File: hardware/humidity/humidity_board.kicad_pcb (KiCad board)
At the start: 2 copper layers, 139 x 20 mm, 23 parts, among them IC1 ATMEGA88-A, J1 RJ45, P1 ISP, P2 UART, SW1 SW_RESET, U1 ST485, U2 HYT271, m3_loch VAL**

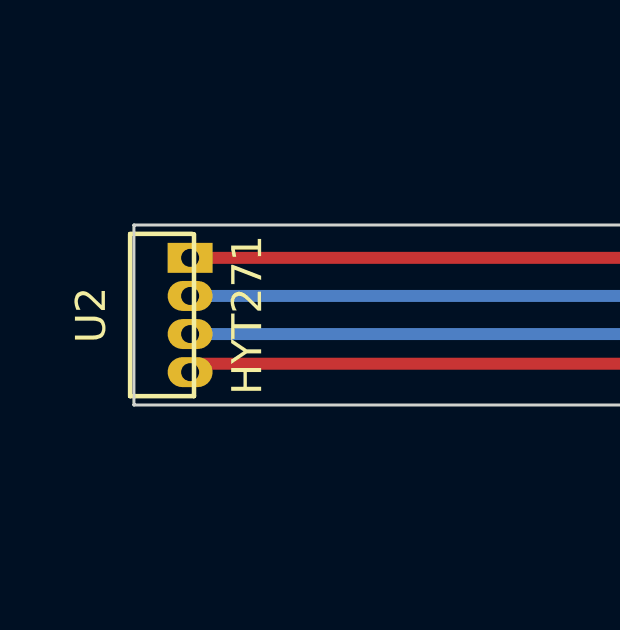
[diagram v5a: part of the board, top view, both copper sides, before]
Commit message: change sensor modules
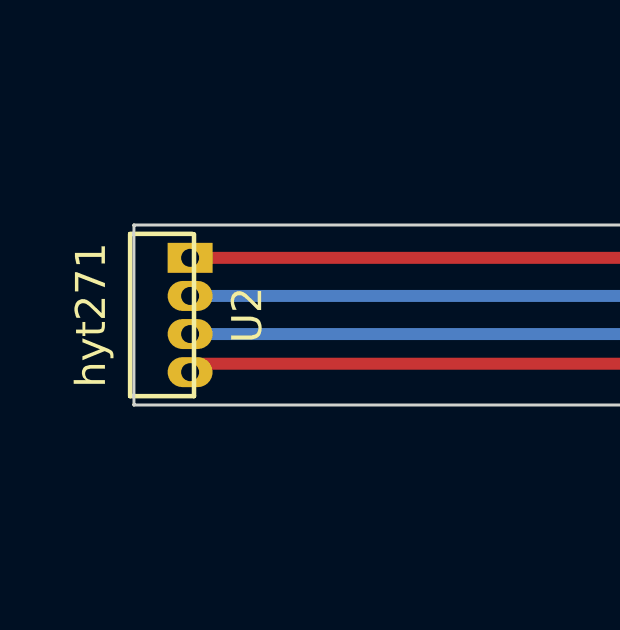
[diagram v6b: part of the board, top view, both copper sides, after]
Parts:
- removed U2: HYT271, HYT271
- added hyt271: U2, HYT271, F.Cu at (80.5, 96.0)
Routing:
- net /SCL: track 52.9 -> 0.00 mm
- net (no net): track 0.00 -> 52.9 mm
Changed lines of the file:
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@@
 (kicad_pcb (version 3) (host pcbnew "(2013-may-18)-stable")
   (general
-    (links 62)
+    (links 58)
     (no_connects 0)
-    (area 7.399999 79.150001 244.600001 118.7)
+    (area 7.399999 74 244.600001 118.7)
     (thickness 1.6)
     (drawings 12)
@@
     (mod_text_size 1 1)
     (mod_text_width 0.15)
-    (pad_size 1 1.5)
+    (pad_size 1 1.7)
     (pad_drill 0.6)
     (pad_to_mask_clearance 0)
@@
     )
   )
+  (module m3_loch (layer F.Cu)
+    (at 187.5 101)
+    (fp_text reference m3_loch (at 0 -5.588) (layer F.SilkS)
+      (effects (font (size 1 1) (thickness 0.15)))
+    )
+    (fp_text value VAL** (at 0 5.842) (layer F.SilkS)
+      (effects (font (size 1 1) (thickness 0.15)))
+    )
+    (pad "" np_thru_hole circle (at 0 0) (size 3.4 3.4) (drill 3.4)
+      (layers *.Cu *.Mask F.SilkS)
+      (clearance 3.3)
+    )
+  )
+  (module m3_loch (layer F.Cu)
+    (at 125.5 91)
+    (fp_text reference m3_loch (at 0 -5.588) (layer F.SilkS)
+      (effects (font (size 1 1) (thickness 0.15)))
+    )
+    (fp_text value VAL** (at 0 5.842) (layer F.SilkS)
+      (effects (font (size 1 1) (thickness 0.15)))
+    )
+    (pad "" np_thru_hole circle (at 0 0) (size 3.4 3.4) (drill 3.4)
+      (layers *.Cu *.Mask F.SilkS)
+      (clearance 3.3)
+    )
+  )
   (module HYT271 (layer F.Cu)
     (at 80.5 96 270)
-    (fp_text reference U2 (at 0 3.429 270) (layer F.SilkS)
+    (fp_text reference hyt271 (at 0 3.429 270) (layer F.SilkS)
       (effects (font (size 1 1) (thickness 0.15)))
     )
-    (fp_text value HYT271 (at 0 -1.778 270) (layer F.SilkS)
+    (fp_text value U2 (at 0 -1.778 270) (layer F.SilkS)
       (effects (font (size 1 1) (thickness 0.15)))
     )
@@
     (pad 2 thru_hole oval (at -0.635 0.127 270) (size 1 1.5) (drill 0.6)
       (layers *.Cu *.Mask F.SilkS)
-      (net 14 GND)
     )
     (pad 3 thru_hole oval (at 0.635 0.127 270) (size 1 1.5) (drill 0.6)
       (layers *.Cu *.Mask F.SilkS)
-      (net 18 VCC)
     )
     (pad 4 thru_hole oval (at 1.905 0.127 270) (size 1 1.5) (drill 0.6)
       (layers *.Cu *.Mask F.SilkS)
-      (net 9 /SCL)
     )
     (pad 1 thru_hole trapezoid (at -1.905 0.127 270) (size 1 1.5) (drill 0.6)
       (layers *.Cu *.Mask F.SilkS)
-      (net 10 /SDA)
-    )
-  )
-  (module m3_loch (layer F.Cu)
-    (at 187.5 101)
-    (fp_text reference m3_loch (at 0 -5.588) (layer F.SilkS)
-      (effects (font (size 1 1) (thickness 0.15)))
-    )
-    (fp_text value VAL** (at 0 5.842) (layer F.SilkS)
-      (effects (font (size 1 1) (thickness 0.15)))
-    )
-    (pad "" np_thru_hole circle (at 0 0) (size 3.4 3.4) (drill 3.4)
-      (layers *.Cu *.Mask F.SilkS)
-      (clearance 3.3)
-    )
-  )
-  (module m3_loch (layer F.Cu)
-    (at 125.5 91)
-    (fp_text reference m3_loch (at 0 -5.588) (layer F.SilkS)
-      (effects (font (size 1 1) (thickness 0.15)))
-    )
-    (fp_text value VAL** (at 0 5.842) (layer F.SilkS)
-      (effects (font (size 1 1) (thickness 0.15)))
-    )
-    (pad "" np_thru_hole circle (at 0 0) (size 3.4 3.4) (drill 3.4)
-      (layers *.Cu *.Mask F.SilkS)
-      (clearance 3.3)
     )
   )
@@
   )
   (gr_line (start 244.5 96) (end 7.5 96) (angle 90) (layer Cmts.User) (width 0.2))
+  (segment (start 133.174 97.62408) (end 80.65392 97.62408) (width 0.4) (layer F.Cu) (net 0) (status 20))
+  (segment (start 80.65392 97.62408) (end 80.373 97.905) (width 0.4) (layer F.Cu) (net 0) (status 30))
   (segment (start 142.7752 100.032) (end 144.032 100.032) (width 0.4) (layer F.Cu) (net 1))
   (segment (start 164.098 97.902) (end 163.5 98.5) (width 0.7) (layer F.Cu) (net 1))
@@
   (segment (start 144.5 92) (end 144.5 97) (width 0.7) (layer B.Cu) (net 8))
   (segment (start 144 91.5) (end 144.5 92) (width 0.7) (layer B.Cu) (net 8))
-  (segment (start 133.174 97.62408) (end 80.65392 97.62408) (width 0.4) (layer F.Cu) (net 9) (status 20))
-  (segment (start 80.65392 97.62408) (end 80.373 97.905) (width 0.4) (layer F.Cu) (net 9) (status 30))
   (segment (start 133.174 96.82652) (end 122.82652 96.82652) (width 0.4) (layer F.Cu) (net 10))
   (segment (start 120.095 94.095) (end 80.373 94.095) (width 0.4) (layer F.Cu) (net 10) (status 20))
@@
   (segment (start 142.782 89.392) (end 143.5 89.392) (width 0.7) (layer F.Cu) (net 17))
   (segment (start 141.945 88.555) (end 142.782 89.392) (width 0.7) (layer F.Cu) (net 17))
-  (segment (start 165.4 96.632) (end 167.632 96.632) (width 0.7) (layer F.Cu) (net 18) (status 400000))
+  (segment (start 165.4 96.632) (end 167.632 96.632) (width 0.7) (layer F.Cu) (net 18))
   (segment (start 167.632 96.632) (end 168.5 97.5) (width 0.7) (layer F.Cu) (net 18))
-  (segment (start 165.4 95.362) (end 167.762 95.362) (width 0.7) (layer F.Cu) (net 18) (status 400000))
+  (segment (start 165.4 95.362) (end 167.762 95.362) (width 0.7) (layer F.Cu) (net 18))
   (segment (start 167.762 95.362) (end 168.5 96.1) (width 0.7) (layer F.Cu) (net 18))
-  (segment (start 171.7 94.092) (end 168.908 94.092) (width 0.7) (layer F.Cu) (net 18) (status 400000))
+  (segment (start 171.7 94.092) (end 168.908 94.092) (width 0.7) (layer F.Cu) (net 18))
   (segment (start 168.908 94.092) (end 168.5 94.5) (width 0.7) (layer F.Cu) (net 18))
-  (segment (start 171.5 91.608) (end 169.092 91.608) (width 0.7) (layer F.Cu) (net 18) (status 400000))
+  (segment (start 171.5 91.608) (end 169.092 91.608) (width 0.7) (layer F.Cu) (net 18))
   (segment (start 169.092 91.608) (end 168.5 92.2) (width 0.7) (layer F.Cu) (net 18))
   (segment (start 169 101) (end 169 98.4) (width 0.7) (layer F.Cu) (net 18))

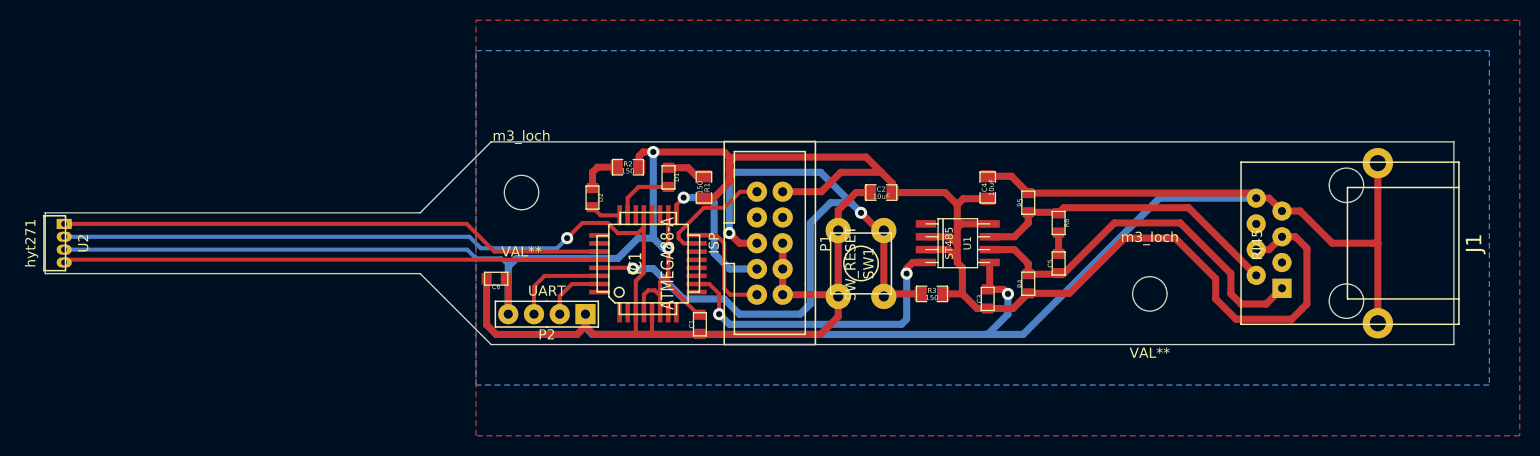
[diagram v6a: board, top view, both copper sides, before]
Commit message: change humidity
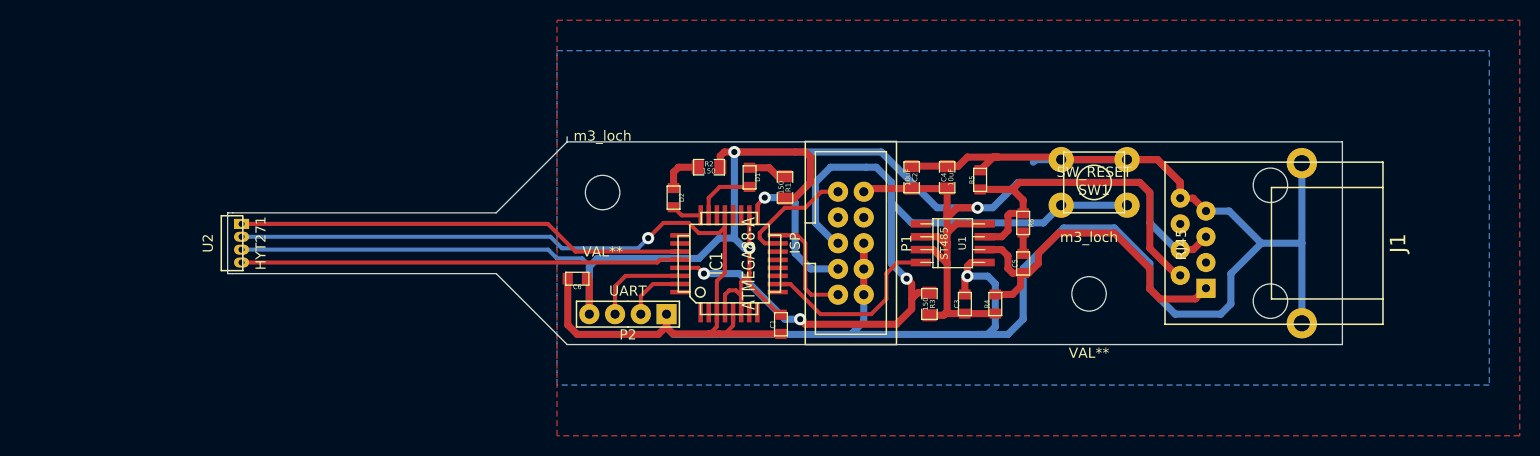
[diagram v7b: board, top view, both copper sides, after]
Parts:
- removed hyt271: U2, HYT271
- added U2: HYT271, HYT271, F.Cu at (98.0, 96.0)
- moved SW1 24.4 mm to (182.0, 90.0), turned to 180 degrees
- moved C1 8.00 mm to (151.1, 104.0)
- moved C6 8.00 mm to (131.0, 99.5)
- moved D1 8.00 mm to (148.0, 89.5)
- moved D2 8.00 mm to (140.5, 91.5)
- moved IC1 8.00 mm to (146.0, 98.0)
- moved P1 8.00 mm to (158.0, 96.0)
- moved P2 8.00 mm to (136.0, 103.0)
- moved R1 8.00 mm to (151.5, 90.5)
- moved R2 8.00 mm to (144.0, 88.5)
- moved m3_loch 8.00 mm to (133.5, 91.0)
- moved J1 7.50 mm to (190.5, 96.0)
- moved m3_loch 6.00 mm to (181.5, 101.0)
- moved R5 5.26 mm to (170.8, 89.8)
- moved C4 4.12 mm to (167.5, 89.5)
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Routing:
- net (no net): track 52.9 -> 0.00 mm
- net /SCL: track 0.00 -> 43.4 mm
- net VCC: track 235.8 -> 208.8 mm, vias 2 -> 3
- net GND: track 294.4 -> 278.7 mm
- net /DI: track 30.9 -> 18.9 mm, vias 2 -> 0
- net /SDA: track 53.9 -> 44.4 mm
- net /RESET: track 72.7 -> 82.2 mm
- net /zb: track 31.0 -> 35.5 mm
- net /za: track 37.7 -> 34.3 mm
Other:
- board size 139 x 20 mm -> 110 x 20.5 mm

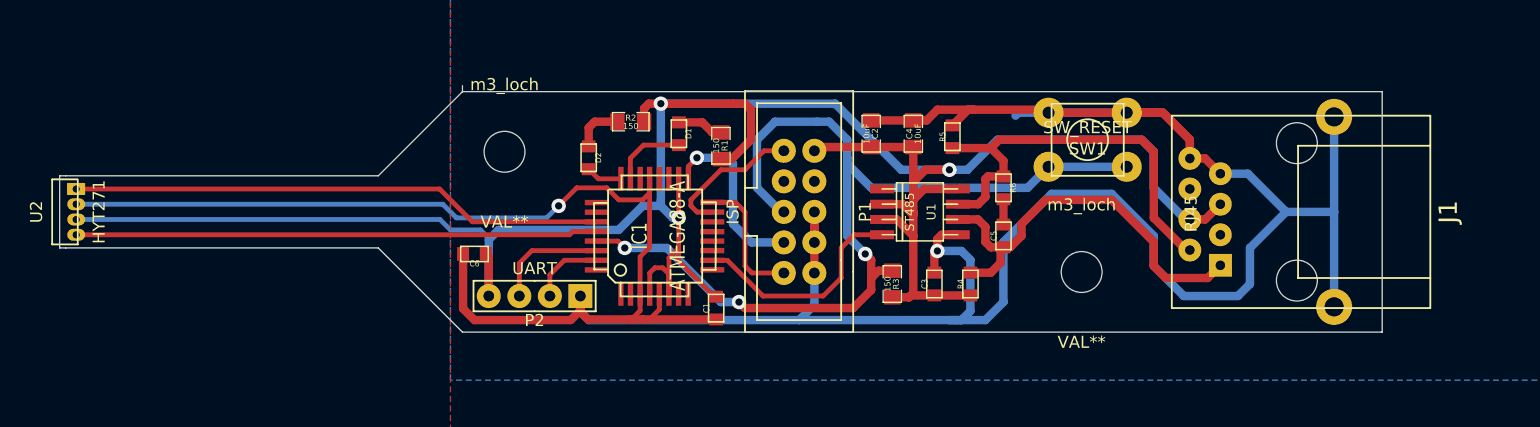
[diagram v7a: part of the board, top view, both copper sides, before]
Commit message: humidity smaller
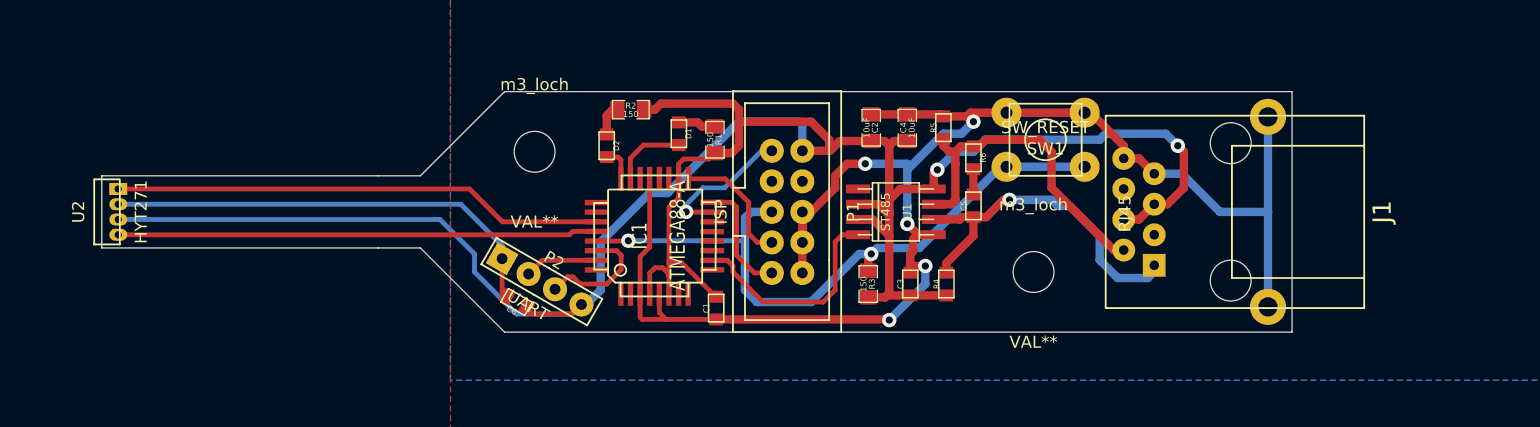
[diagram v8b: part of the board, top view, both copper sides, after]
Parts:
- moved J1 5.50 mm to (185.0, 96.0)
- moved C6 5.32 mm to (134.5, 103.5), turned to 150 degrees
- moved m3_loch 4.00 mm to (177.5, 101.0)
- moved C5 3.54 mm to (172.5, 95.5)
- moved R6 3.54 mm to (172.5, 91.5)
- moved SW1 3.50 mm to (178.5, 90.0)
- moved U2 3.50 mm to (101.5, 96.0)
- moved m3_loch 2.50 mm to (136.0, 91.0)
- moved C3 2.00 mm to (167.2, 102.0)
- moved R3 2.00 mm to (163.8, 102.0)
- moved R4 2.00 mm to (170.2, 102.0)
- moved U1 2.00 mm to (168.0, 96.0)
- moved D2 1.80 mm to (142.0, 90.5)
- moved P2 1.34 mm to (136.6, 101.8), turned to 330 degrees
- moved R5 1.06 mm to (170.0, 89.0)
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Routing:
- net GND: track 278.7 -> 170.8 mm, vias 2 -> 5
- net /RESET: track 82.2 -> 55.8 mm, vias 3 -> 2
- net VCC: track 208.8 -> 196.3 mm, vias 3 -> 2
- net /zb: track 35.5 -> 27.7 mm
- net /za: track 34.3 -> 29.2 mm, vias 0 -> 1
- net /SCK: track 15.1 -> 10.7 mm, vias 1 -> 0
- net /SDA: track 44.4 -> 40.9 mm
- net /SCL: track 43.4 -> 39.9 mm
- net N-0000015: track 4.15 -> 2.65 mm
- net /MISO: track 11.0 -> 9.73 mm
- net N-0000016: track 3.85 -> 3.14 mm
- net /MOSI: track 11.9 -> 11.8 mm, vias 0 -> 1
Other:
- board size 110 x 20.5 mm -> 99 x 20 mm
